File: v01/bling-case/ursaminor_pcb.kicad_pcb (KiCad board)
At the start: 2 copper layers, 298.6 x 118.1 mm, 210 parts, among them J1 USB_C_Receptacle_USB2.0, J2 I2C-L, J3 I2C-R, J4 AVR-ISP-6, SW1 Reset, U1 ATmega32U4-AU, U2 MCP23017_SO, U3 IS31FL3733-TQ, U4 IS31FL3733-TQ, U5 PRTR5V0U2X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

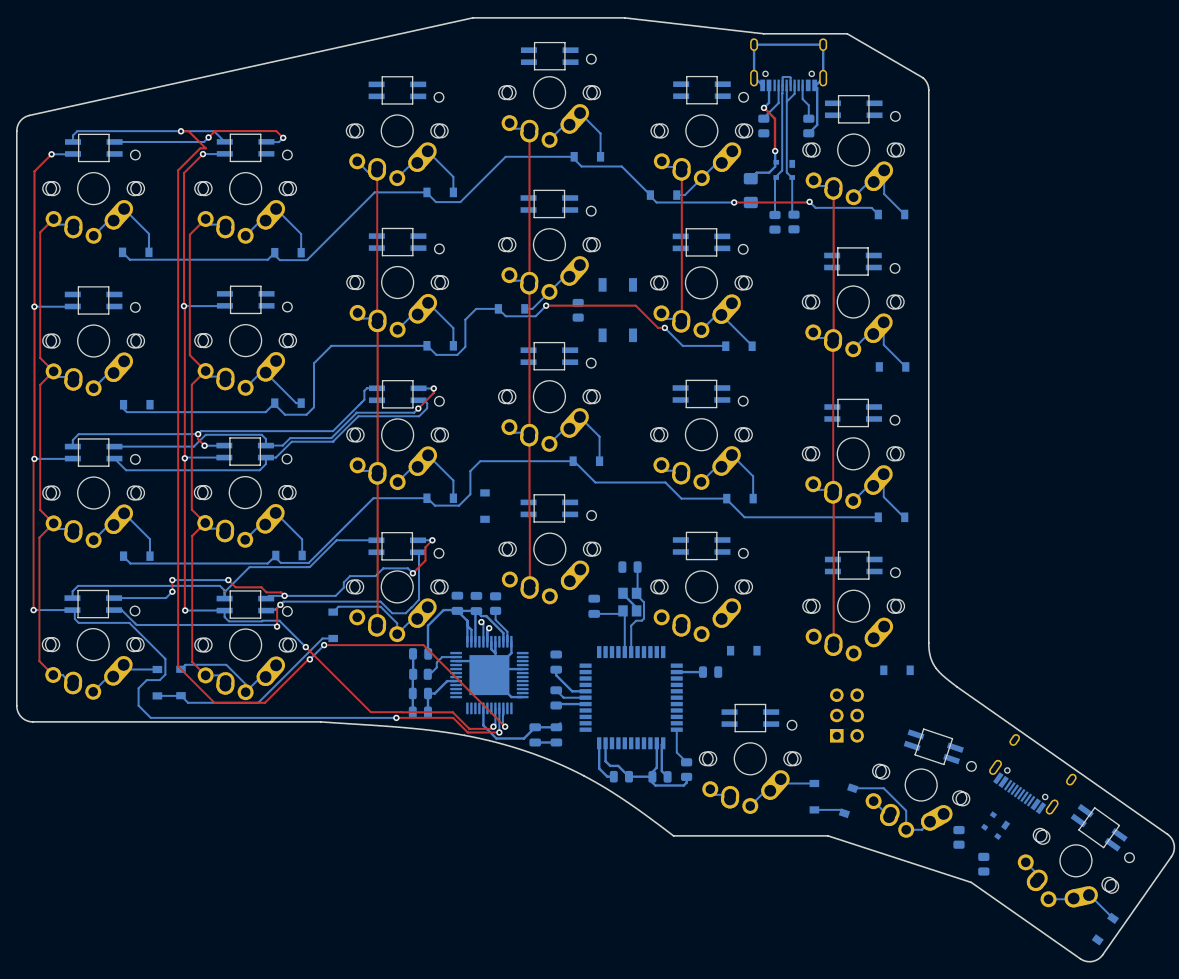
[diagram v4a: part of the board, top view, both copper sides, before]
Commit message: Get RGB matrix on left side roughly routed
If I can get the left side to work, the right should be easier.
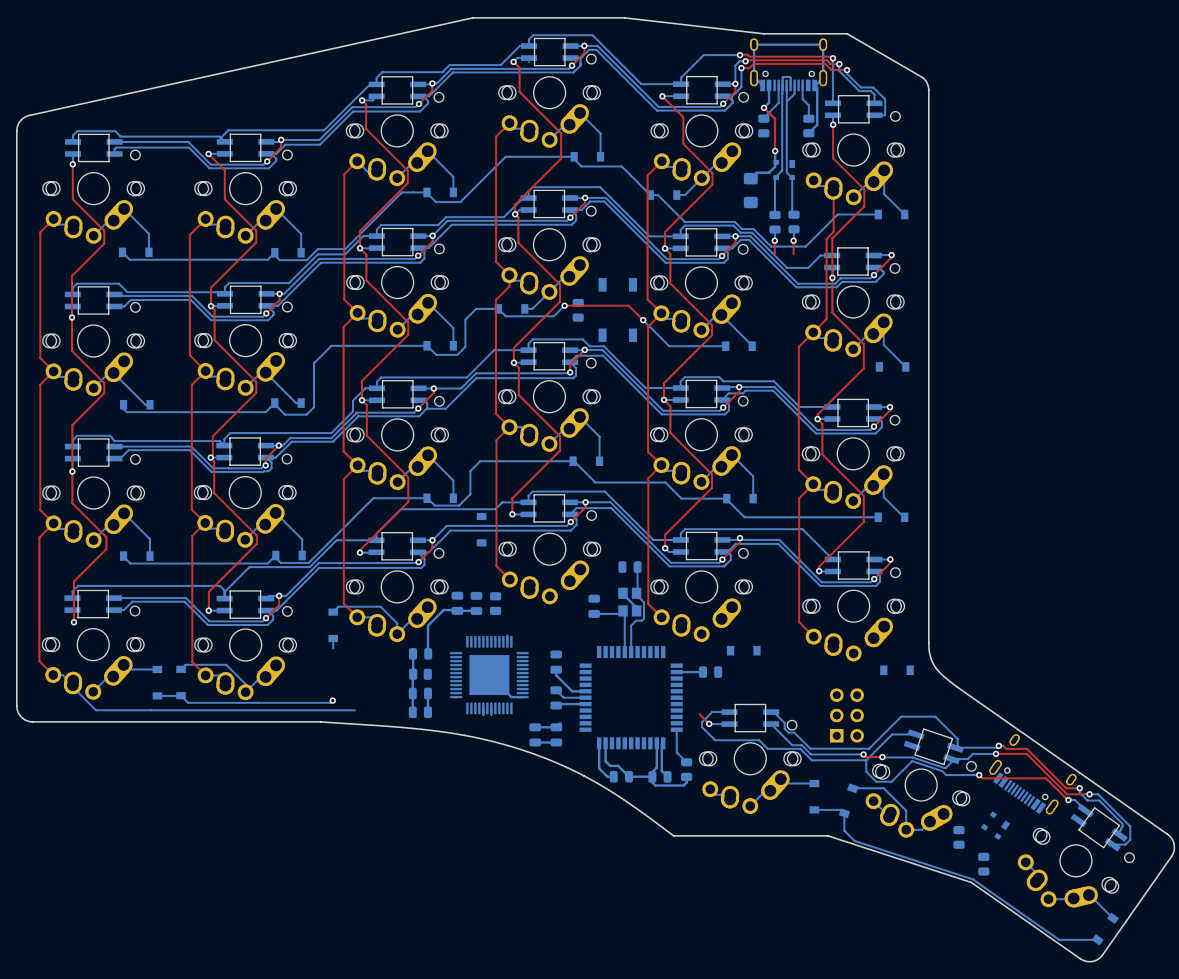
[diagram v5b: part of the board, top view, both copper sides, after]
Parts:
- moved D22 2.98 mm to (72.0, 79.9)
- moved D58 0.52 mm to (80.5, 25.2)
- turned U4 to 0 degrees
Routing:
- net Left-SW3: track 43.8 -> 176.6 mm, vias 0 -> 2
- net Left-SW2: track 51.4 -> 180.8 mm, vias 6 -> 12
- net Left-SW10: track 0.00 -> 127.4 mm, vias 0 -> 2
- net Left-SW1: track 51.3 -> 175.4 mm, vias 2 -> 4
- net Left-SW8: track 0.00 -> 123.8 mm, vias 0 -> 10
- net Left-SW7: track 0.00 -> 120.6 mm
- net Left-SW9: track 0.00 -> 109.9 mm
- net Left-SW11: track 24.3 -> 121.9 mm, vias 2 -> 10
- net Left-CS5: track 0.00 -> 79.9 mm, vias 0 -> 4
- net Left-CS3: track 0.00 -> 79.2 mm, vias 0 -> 4
- net Left-CS4: track 0.00 -> 78.9 mm, vias 0 -> 4
- net Left-SW5: track 46.8 -> 123.6 mm, vias 2 -> 10
- net Left-SW4: track 45.3 -> 120.0 mm
- net Left-CS1: track 147.5 -> 73.3 mm, vias 6 -> 4
- net Left-CS6: track 0.19 -> 74.1 mm, vias 0 -> 4
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
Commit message: More routing progress.
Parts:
- moved J4 103.3 mm to (49.3, 25.6), turned to 0 degrees
- moved C1 23.6 mm to (109.6, 98.5), turned to 90 degrees
- moved D22 18.9 mm to (88.8, 88.6)
- moved C5 18.4 mm to (97.7, 115.8)
- moved Y1 17.9 mm to (105.6, 98.6), turned to 180 degrees
- moved C2 17.9 mm to (101.5, 98.5), turned to 270 degrees
- moved C6 15.7 mm to (82.6, 96.7), turned to 180 degrees
- moved C4 13.4 mm to (81.4, 107.3)
- moved C7 10.7 mm to (91.7, 93.8), turned to 0 degrees
- moved C3 9.23 mm to (87.2, 93.8), turned to 180 degrees
- moved R8 5.50 mm to (93.6, 113.6), turned to 180 degrees
- moved C12 5.10 mm to (81.3, 100.4), turned to 180 degrees
- moved D23 4.42 mm to (107.8, 91.8), turned to 90 degrees
- moved C18 3.07 mm to (81.3, 103.9), turned to 180 degrees
- moved U1 2.98 mm to (91.3, 103.8), turned to 270 degrees
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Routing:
- net +5V: track 34.7 -> 262.0 mm, vias 0 -> 8
- net Col0: track 110.0 -> 257.7 mm, vias 0 -> 3
- net Col5: track 71.9 -> 188.1 mm, vias 0 -> 3
- net Col1: track 72.6 -> 188.4 mm, vias 0 -> 4
- net Row3-L: track 23.6 -> 130.9 mm, vias 1 -> 2
- net Col4: track 72.5 -> 166.8 mm, vias 0 -> 2
- net SDA-L: track 0.00 -> 91.0 mm, vias 0 -> 4
- net SCL-L: track 0.85 -> 90.7 mm, vias 0 -> 3
- net Left-SW3: track 176.6 -> 265.7 mm, vias 2 -> 6
- net Row1-L: track 91.8 -> 171.6 mm, vias 2 -> 4
- net Left-CS9: track 0.00 -> 79.2 mm, vias 0 -> 1
- net D-: track 3.05 -> 80.0 mm, vias 1 -> 4
- net D+: track 3.15 -> 80.0 mm, vias 1 -> 4
- net Row0-L: track 108.6 -> 184.1 mm, vias 0 -> 2
- net Left-CS1: track 73.3 -> 146.5 mm, vias 4 -> 5
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
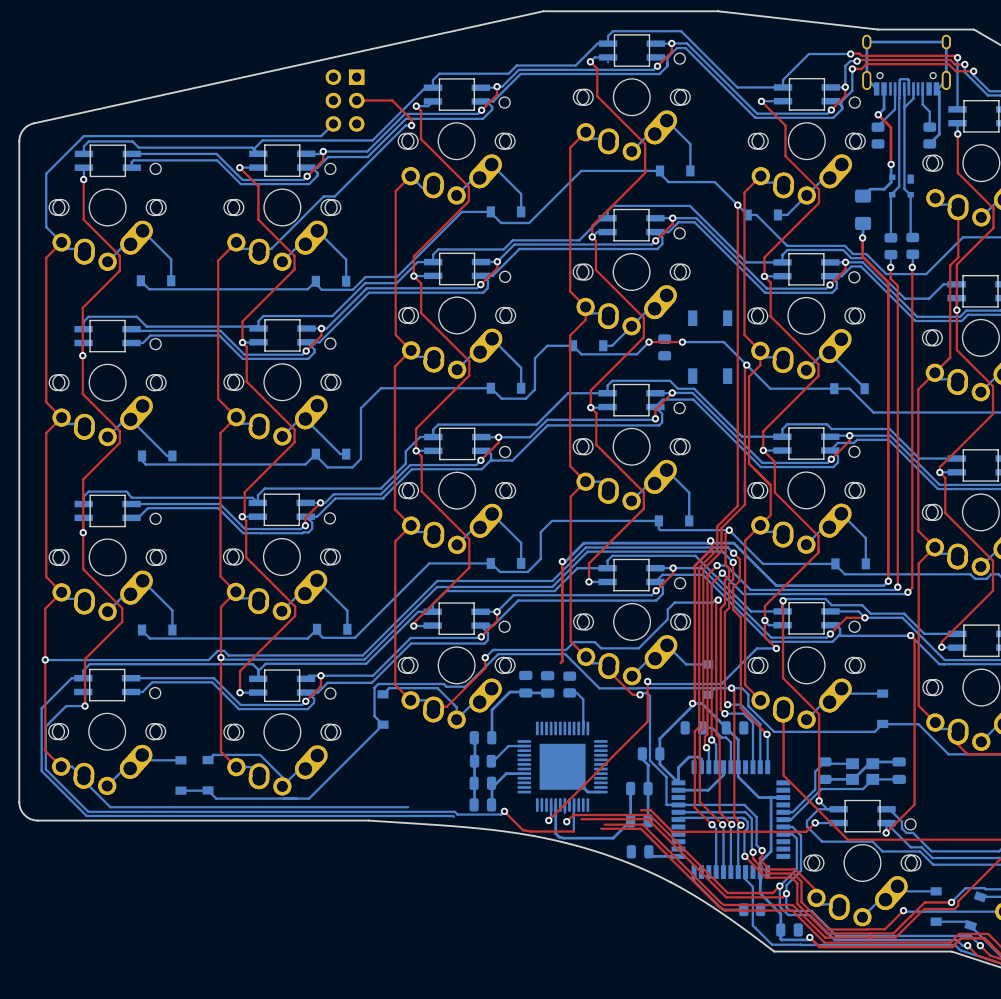
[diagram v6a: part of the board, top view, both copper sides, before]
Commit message: Routing MCU and LED driver
* Roughly finished on the MCU. I think components are still close to the
  required pins.
* Starting to routes traces out of LED driver to the matrix lines. I had
  to rotate the driver and this caused a relayout of the surrounding
  area.
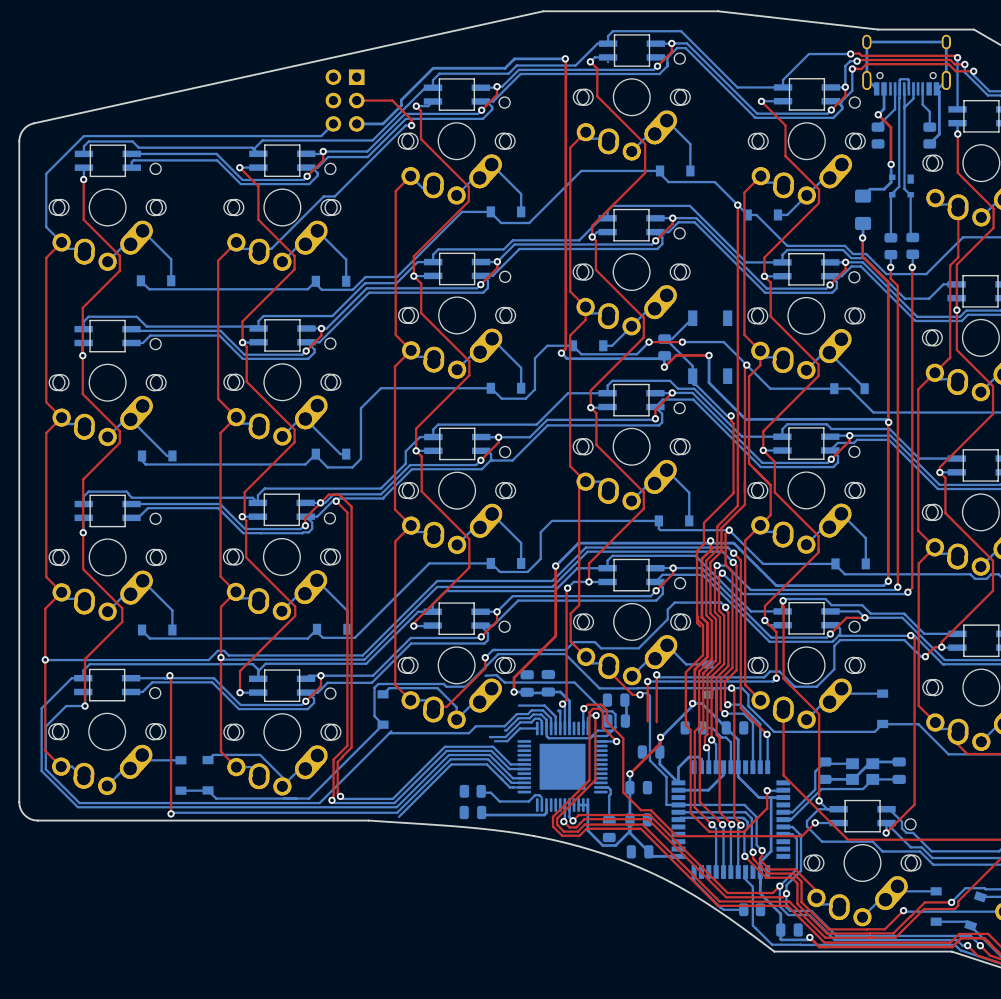
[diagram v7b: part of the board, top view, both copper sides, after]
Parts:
- moved C13 18.4 mm to (78.8, 90.8)
- moved C19 16.1 mm to (78.8, 93.1)
- moved R12 15.7 mm to (63.2, 100.7), turned to 180 degrees
- moved R14 15.6 mm to (78.0, 104.8), turned to 270 degrees
- moved C11 8.20 mm to (63.2, 103.0)
- moved C17 2.45 mm to (71.4, 89.0)
- moved C21 2.23 mm to (69.1, 89.0)
- moved C6 0.20 mm to (82.6, 96.5)
- moved C12 0.12 mm to (81.2, 100.3)
- moved C18 0.12 mm to (81.2, 103.8)
- turned U4 to 0 degrees
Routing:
- net +5V: track 262.0 -> 385.6 mm, vias 8 -> 16
- net Net-(J4-Pad5): track 0.00 -> 77.4 mm, vias 0 -> 2
- net Left-SW5: track 123.6 -> 183.4 mm, vias 10 -> 11
- net Left-SW4: track 120.0 -> 177.9 mm, vias 0 -> 2
- net Left-SW2: track 203.0 -> 260.7 mm, vias 12 -> 14
- net Left-CS6: track 74.1 -> 116.0 mm, vias 4 -> 6
- net Col0: track 257.7 -> 220.7 mm
- net Left-SW12: track 114.4 -> 149.8 mm
- net Left-CS9: track 79.2 -> 106.6 mm, vias 1 -> 2
- net Left-CS8: track 58.3 -> 79.9 mm, vias 1 -> 2
- net GND: track 79.0 -> 59.0 mm
- net Left-CS7: track 22.9 -> 41.6 mm, vias 1 -> 2
- net Left-CS4: track 78.9 -> 97.1 mm, vias 4 -> 6
- net Left-SW1: track 198.0 -> 215.3 mm
- net Left-CS5: track 120.8 -> 105.4 mm, vias 7 -> 6
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
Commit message: Almost done routing the left side.
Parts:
- turned C5 to 180 degrees
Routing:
- net Left-SW10: track 132.6 -> 217.3 mm, vias 2 -> 4
- net GND: track 59.0 -> 138.4 mm, vias 0 -> 99
- net Left-SW11: track 129.3 -> 207.5 mm, vias 10 -> 11
- net Left-SW8: track 123.8 -> 197.3 mm, vias 10 -> 11
- net Left-SW9: track 109.9 -> 182.7 mm, vias 0 -> 2
- net Left-SW7: track 120.6 -> 193.2 mm, vias 0 -> 2
- net Net-(J4-Pad5): track 77.4 -> 148.7 mm, vias 2 -> 3
- net Left-CS2: track 84.8 -> 155.0 mm, vias 4 -> 7
- net Row2-L: track 137.0 -> 203.8 mm, vias 2 -> 3
- net Left-SW6: track 109.4 -> 165.3 mm, vias 0 -> 2
- net Left-SW12: track 149.8 -> 198.6 mm, vias 2 -> 4
- net Left-CS3: track 81.5 -> 109.3 mm, vias 4 -> 5
- net +5V: track 385.6 -> 411.3 mm
- net Left-SW1: track 215.3 -> 234.0 mm, vias 4 -> 6
- net Left-CS5: track 105.4 -> 115.4 mm, vias 6 -> 7
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- added copper zone on B.Cu, net GND
- added copper zone on F.Cu, net GND
